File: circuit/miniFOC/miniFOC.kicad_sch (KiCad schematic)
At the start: 61 parts, among them J1 Conn_01x05, J2 Conn_01x06, J3 Conn_01x02, J4 Conn_01x01, J5 Conn_01x01, J6 Conn_01x01, U1 XC6206P332MR, U2 AT32F421C8, U3 LM321, U4 COS722MR, U5 uP9636, U6 uP9636, U7 JW5017S, U8 uP9636

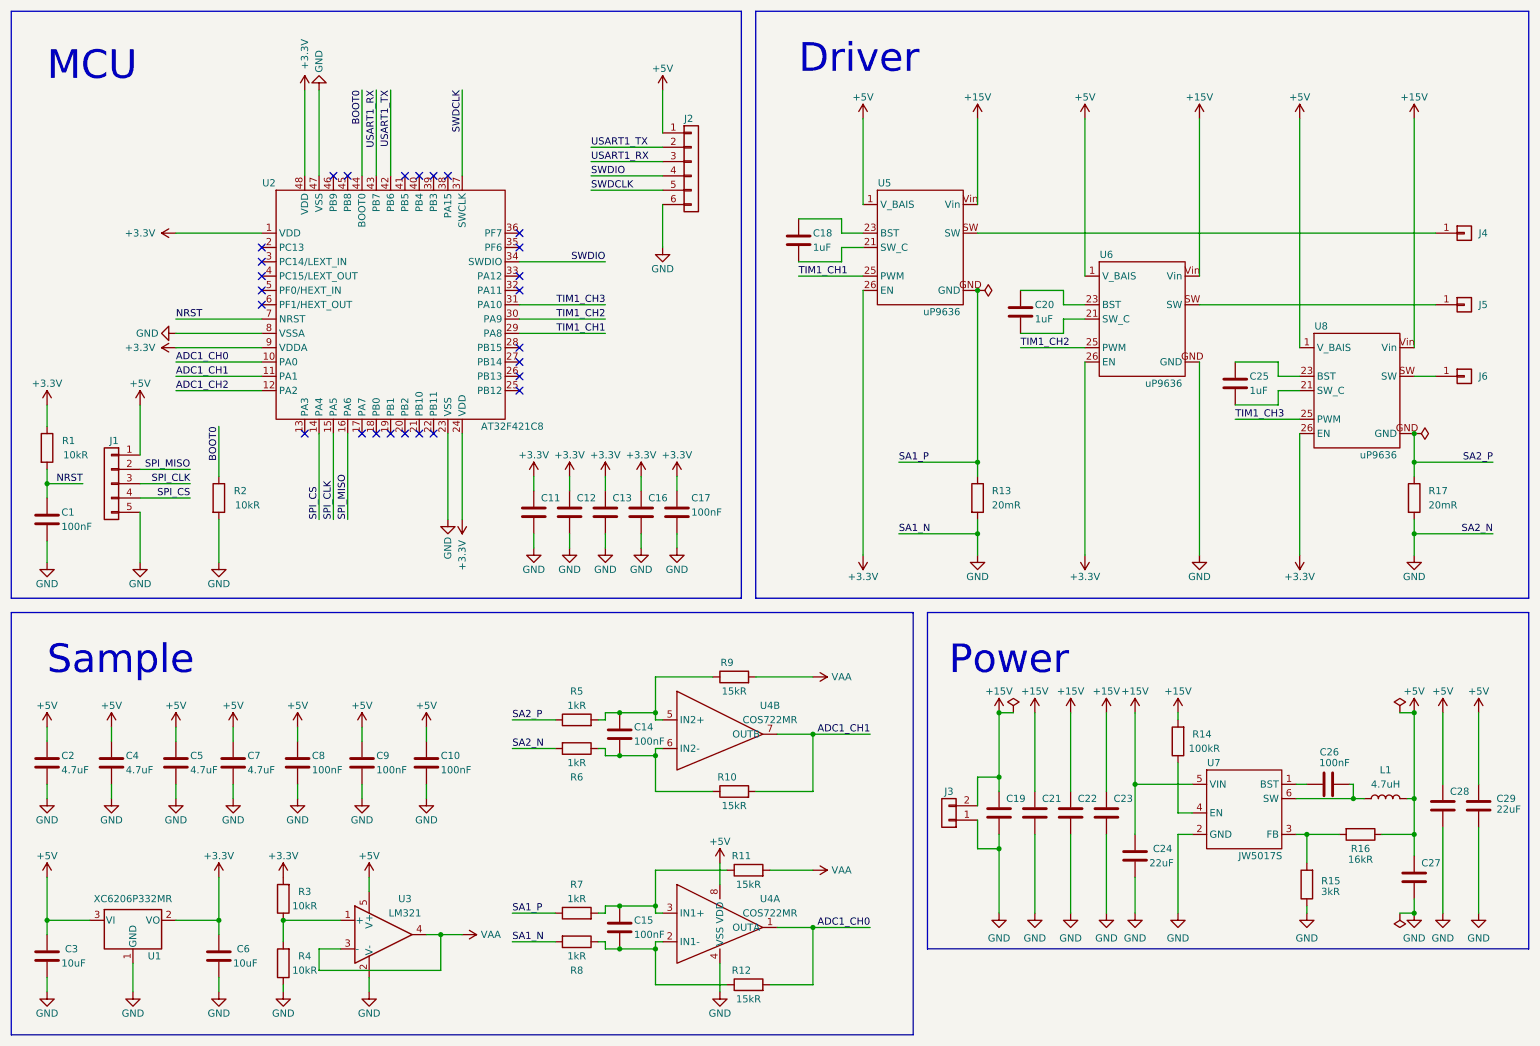
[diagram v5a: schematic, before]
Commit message: Complete the circuit and PCB design for version 2.0.
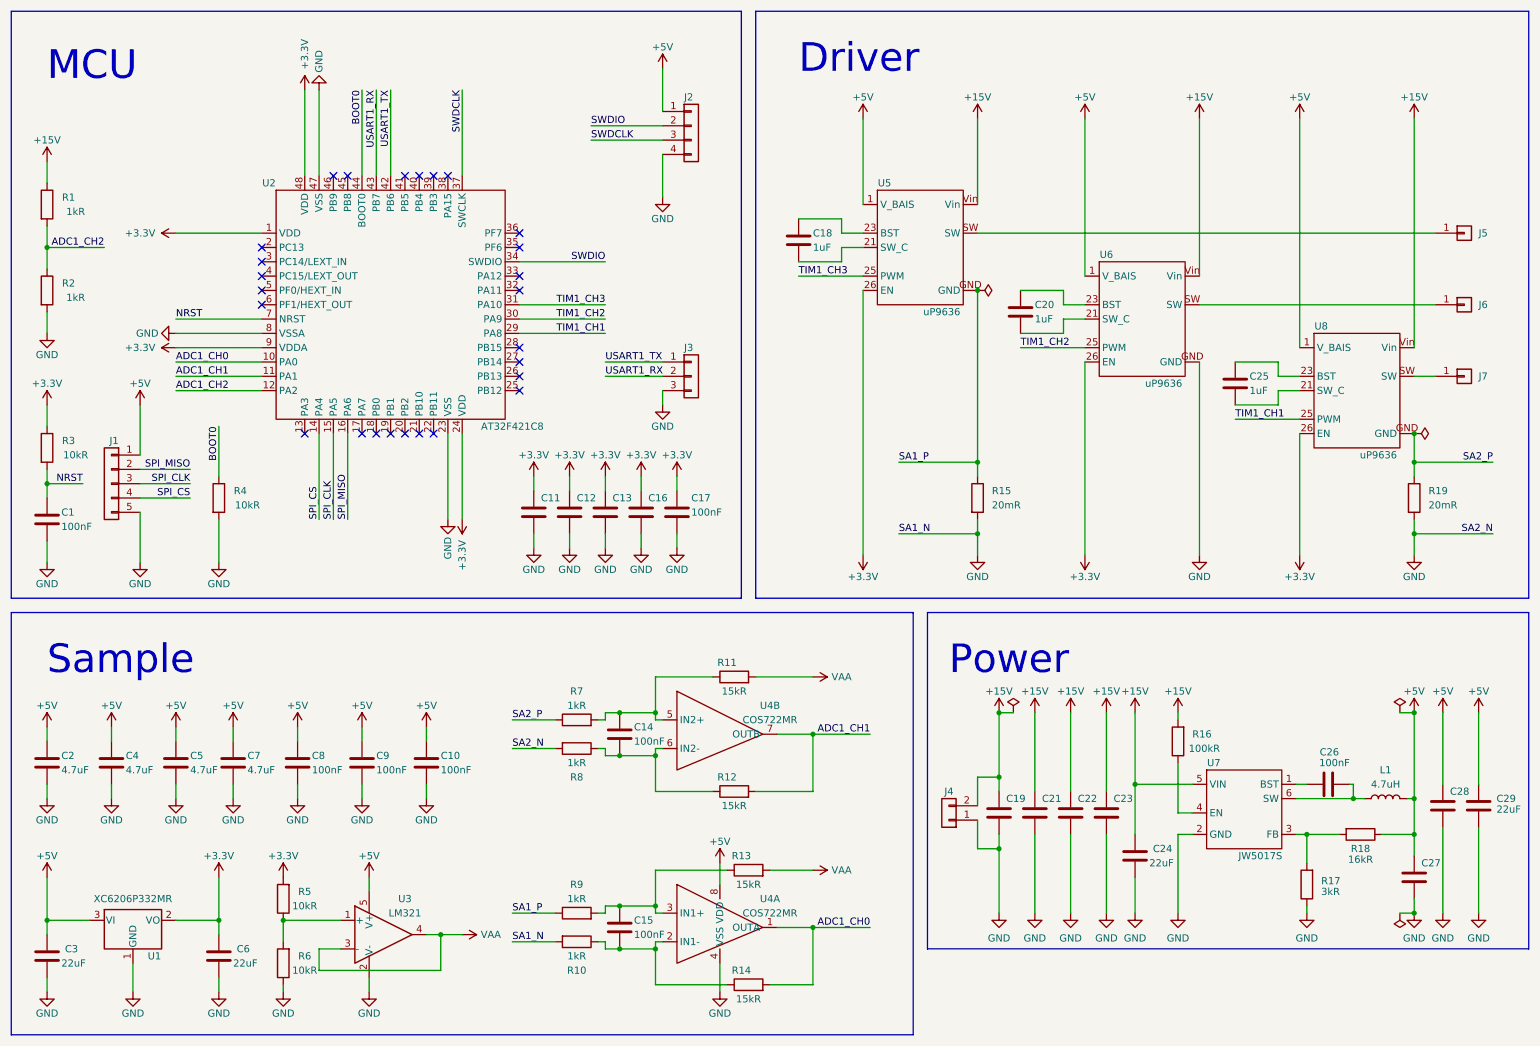
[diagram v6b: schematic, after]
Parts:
- removed J2: Conn_01x06, Connector_JST:JST_GH_SM06B-GHS-TB_1x06-1MP_P1.25mm_Horizontal, symbol Connector_Generic:Conn_01x06
- added J2: Conn_01x04, Library:Pad_4, symbol Connector_Generic:Conn_01x04
- added J3: Conn_01x03, Library:JST_GH_SM03B-GHS-TB_1x03-1MP_P1.25mm_Horizontal, symbol Connector_Generic:Conn_01x03
- added R1, R2: 1kR, Library:R_0402_1005Metric, symbol Device:R
- C1, C10, C11, C12, C13, C14, C15, C16, C17, C18, C2, C20, C25, C26, C4, C5, C7, C8, C9: footprint Capacitor_SMD:C_0402_1005Metric -> Library:C_0402_1005Metric
- C19, C21, C22, C23, C24: footprint Capacitor_SMD:C_0805_2012Metric -> Library:C_0805_2012Metric
- C27, C28, C29: footprint Capacitor_SMD:C_0603_1608Metric -> Library:C_0603_1608Metric
- C3, C6: value 10uF -> 22uF; footprint Capacitor_SMD:C_0603_1608Metric -> Library:C_0603_1608Metric
- J1: footprint Connector_JST:JST_GH_SM05B-GHS-TB_1x05-1MP_P1.25mm_Horizontal -> Library:Pad_5
- J4: renamed from J3; footprint Connector_Wire:SolderWire-0.1sqmm_1x02_P3.6mm_D0.4mm_OD1mm -> Library:SolderWire-0.1sqmm_1x02_P3.6mm_D0.4mm_OD1mm
- J5: renamed from J4; footprint Connector_PinHeader_2.54mm:PinHeader_1x01_P2.54mm_Vertical -> Library:Pad_1
- J6: renamed from J5; footprint Connector_PinHeader_2.54mm:PinHeader_1x01_P2.54mm_Vertical -> Library:Pad_1
- J7: renamed from J6; footprint Connector_PinHeader_2.54mm:PinHeader_1x01_P2.54mm_Vertical -> Library:Pad_1
- L1: footprint Inductor_SMD:L_Coilcraft_XxL4040 -> Library:L_Coilcraft_XxL4040
- R10: renamed from R8; footprint Resistor_SMD:R_0402_1005Metric -> Library:R_0402_1005Metric
- R11: renamed from R9; footprint Resistor_SMD:R_0402_1005Metric -> Library:R_0402_1005Metric
- R12: renamed from R10; footprint Resistor_SMD:R_0402_1005Metric -> Library:R_0402_1005Metric
- R13: renamed from R11; footprint Resistor_SMD:R_0402_1005Metric -> Library:R_0402_1005Metric
- R14: renamed from R12; footprint Resistor_SMD:R_0402_1005Metric -> Library:R_0402_1005Metric
- R15: renamed from R13; footprint Resistor_SMD:R_0805_2012Metric -> Library:R_0805_2012Metric
- R16: renamed from R14; footprint Capacitor_SMD:C_0402_1005Metric -> Library:R_0402_1005Metric
- R17: renamed from R15; footprint Capacitor_SMD:C_0402_1005Metric -> Library:R_0402_1005Metric
- R18: renamed from R16; footprint Capacitor_SMD:C_0402_1005Metric -> Library:R_0402_1005Metric
- R19: renamed from R17; footprint Resistor_SMD:R_0805_2012Metric -> Library:R_0805_2012Metric
- R3: renamed from R1; footprint Resistor_SMD:R_0402_1005Metric -> Library:R_0402_1005Metric
- R4: renamed from R2; footprint Resistor_SMD:R_0402_1005Metric -> Library:R_0402_1005Metric
- R5: renamed from R3; footprint Resistor_SMD:R_0402_1005Metric -> Library:R_0402_1005Metric
- R6: renamed from R4; footprint Resistor_SMD:R_0402_1005Metric -> Library:R_0402_1005Metric
- R7: renamed from R5; footprint Resistor_SMD:R_0402_1005Metric -> Library:R_0402_1005Metric
- R8: renamed from R6; footprint Resistor_SMD:R_0402_1005Metric -> Library:R_0402_1005Metric
- R9: renamed from R7; footprint Resistor_SMD:R_0402_1005Metric -> Library:R_0402_1005Metric
- U1: footprint Package_TO_SOT_SMD:SOT-23 -> Library:SOT-23
- U2: footprint Package_QFP:LQFP-48_7x7mm_P0.5mm -> Library:LQFP-48_7x7mm_P0.5mm
- U3: footprint Package_TO_SOT_SMD:SOT-23-5 -> Library:SOT-23-5
- U4: footprint Package_SO:MSOP-8_3x3mm_P0.65mm -> Library:MSOP-8_3x3mm_P0.65mm
- U7: footprint Package_TO_SOT_SMD:SOT-23-6 -> Library:SOT-23-6
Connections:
- net +15V: now also R1.1
- net +5V: now also J2.1 (Pin_1)
- net ADC1_CH2: now also R1.2, R2.1
- net GND: now also J2.4 (Pin_4), J3.3 (Pin_3), R2.2
- net SWDCLK: now also J2.3 (Pin_3)
- net SWDIO: now also J2.2 (Pin_2)
- net TIM1_CH1: now also U8.25 (PWM); no longer U5.25 (PWM)
- net TIM1_CH3: now also U5.25 (PWM); no longer U8.25 (PWM)
- net USART1_RX: now also J3.2 (Pin_2)
- net USART1_TX: now also J3.1 (Pin_1)

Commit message: Mosify miniFOC schematic, using new scheme
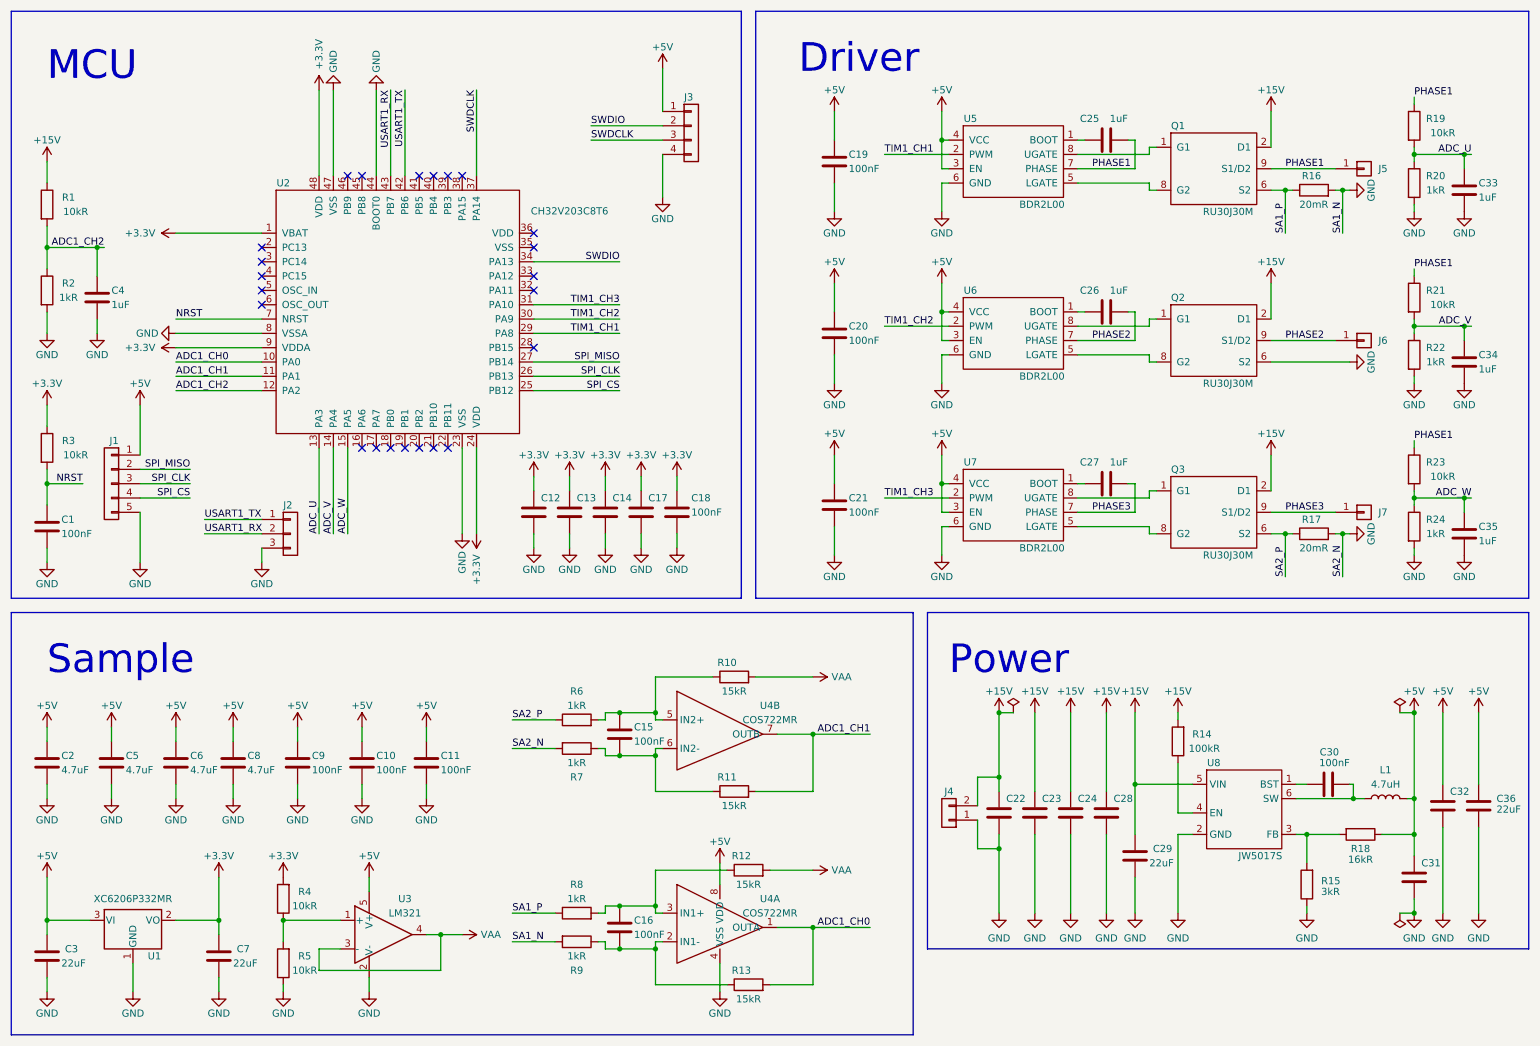
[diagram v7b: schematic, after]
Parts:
- removed C18, C20, C25: 1uF, Library:C_0402_1005Metric, symbol Device:C
- removed R19: 20mR, Library:R_0805_2012Metric, symbol Device:R
- removed R4: 10kR, Library:R_0402_1005Metric, symbol Device:R
- removed U2: AT32F421C8, Library:LQFP-48_7x7mm_P0.5mm, symbol Library:AT32F421C8
- removed U5, U6, U8: uP9636, Library:QFN-26_4040_IPS, symbol Library:uP9636
- added C19, C20, C21: 100nF, library:C_0402_1005Metric, symbol library:C
- added C25, C26, C27, C33, C34, C35, C4: 1uF, library:C_0402_1005Metric, symbol library:C
- added Q1, Q2, Q3: RU30J30M, library:PDFN-8_L5.8-W4.9_RU30J30M, symbol library:RU30J30M
- added R17: 20mR, library:R_0805_2012Metric, symbol library:R
- added R19, R21, R23: 10kR, library:R_0402_1005Metric, symbol library:R
- added R20, R22, R24: 1kR, library:R_0402_1005Metric, symbol library:R
- added U2: CH32V203C8T6, library:LQFP-48_7x7mm_P0.5mm, symbol library:CH32V203C8T6
- added U5, U6, U7: BDR2L00, library:TDFN-8_L2.0-W2.0-P0.50-BL-EP, symbol library:BDR2L00
- C1, C2: footprint Library:C_0402_1005Metric -> library:C_0402_1005Metric; symbol Device:C -> library:C
- C10: renamed from C9; footprint Library:C_0402_1005Metric -> library:C_0402_1005Metric; symbol Device:C -> library:C
- C11: renamed from C10; footprint Library:C_0402_1005Metric -> library:C_0402_1005Metric; symbol Device:C -> library:C
- C12: renamed from C11; footprint Library:C_0402_1005Metric -> library:C_0402_1005Metric; symbol Device:C -> library:C
- C13: renamed from C12; footprint Library:C_0402_1005Metric -> library:C_0402_1005Metric; symbol Device:C -> library:C
- C14: renamed from C13; footprint Library:C_0402_1005Metric -> library:C_0402_1005Metric; symbol Device:C -> library:C
- C15: renamed from C14; footprint Library:C_0402_1005Metric -> library:C_0402_1005Metric; symbol Device:C -> library:C
- C16: renamed from C15; footprint Library:C_0402_1005Metric -> library:C_0402_1005Metric; symbol Device:C -> library:C
- C17: renamed from C16; footprint Library:C_0402_1005Metric -> library:C_0402_1005Metric; symbol Device:C -> library:C
- C18: renamed from C17; footprint Library:C_0402_1005Metric -> library:C_0402_1005Metric; symbol Device:C -> library:C
- C22: renamed from C19; footprint Library:C_0805_2012Metric -> library:C_0805_2012Metric; symbol Device:C -> library:C
- C23: renamed from C21; footprint Library:C_0805_2012Metric -> library:C_0805_2012Metric; symbol Device:C -> library:C
- C24: renamed from C22; footprint Library:C_0805_2012Metric -> library:C_0805_2012Metric; symbol Device:C -> library:C
- C28: renamed from C23; footprint Library:C_0805_2012Metric -> library:C_0805_2012Metric; symbol Device:C -> library:C
- C29: renamed from C24; footprint Library:C_0805_2012Metric -> library:C_0805_2012Metric; symbol Device:C -> library:C
- C3: footprint Library:C_0603_1608Metric -> library:C_0603_1608Metric; symbol Device:C -> library:C
- C30: renamed from C26; footprint Library:C_0402_1005Metric -> library:C_0402_1005Metric; symbol Device:C -> library:C
- C31: renamed from C27; footprint Library:C_0603_1608Metric -> library:C_0603_1608Metric; symbol Device:C -> library:C
- C32: renamed from C28; footprint Library:C_0603_1608Metric -> library:C_0603_1608Metric; symbol Device:C -> library:C
- C36: renamed from C29; footprint Library:C_0603_1608Metric -> library:C_0603_1608Metric; symbol Device:C -> library:C
- C5: renamed from C4; footprint Library:C_0402_1005Metric -> library:C_0402_1005Metric; symbol Device:C -> library:C
- C6: renamed from C5; footprint Library:C_0402_1005Metric -> library:C_0402_1005Metric; symbol Device:C -> library:C
- C7: renamed from C6; footprint Library:C_0603_1608Metric -> library:C_0603_1608Metric; symbol Device:C -> library:C
- C8: renamed from C7; footprint Library:C_0402_1005Metric -> library:C_0402_1005Metric; symbol Device:C -> library:C
- C9: renamed from C8; footprint Library:C_0402_1005Metric -> library:C_0402_1005Metric; symbol Device:C -> library:C
- J1: footprint Library:Pad_5 -> library:Pad_5; symbol Connector_Generic:Conn_01x05 -> library:Conn_01x05
- J2: renamed from J3; footprint Library:JST_GH_SM03B-GHS-TB_1x03-1MP_P1.25mm_Horizontal -> library:JST_GH_SM03B-GHS-TB_1x03-1MP_P1.25mm_Horizontal; symbol Connector_Generic:Conn_01x03 -> library:Conn_01x03
- J3: renamed from J2; footprint Library:Pad_4 -> library:Pad_4; symbol Connector_Generic:Conn_01x04 -> library:Conn_01x04
- J4: footprint Library:SolderWire-0.1sqmm_1x02_P3.6mm_D0.4mm_OD1mm -> library:SolderWire-0.1sqmm_1x02_P3.6mm_D0.4mm_OD1mm; symbol Connector_Generic:Conn_01x02 -> library:Conn_01x02
- J5, J6, J7: footprint Library:Pad_1 -> library:Pad_1; symbol Connector_Generic:Conn_01x01 -> library:Conn_01x01
- L1: footprint Library:L_Coilcraft_XxL4040 -> library:L_Coilcraft_XxL4040; symbol Device:L -> library:L
- R1: value 1kR -> 10kR; footprint Library:R_0402_1005Metric -> library:R_0402_1005Metric; symbol Device:R -> library:R
- R10: renamed from R11; footprint Library:R_0402_1005Metric -> library:R_0402_1005Metric; symbol Device:R -> library:R
- R11: renamed from R12; footprint Library:R_0402_1005Metric -> library:R_0402_1005Metric; symbol Device:R -> library:R
- R12: renamed from R13; footprint Library:R_0402_1005Metric -> library:R_0402_1005Metric; symbol Device:R -> library:R
- R13: renamed from R14; footprint Library:R_0402_1005Metric -> library:R_0402_1005Metric; symbol Device:R -> library:R
- R14: renamed from R16; footprint Library:R_0402_1005Metric -> library:R_0402_1005Metric; symbol Device:R -> library:R
- R15: renamed from R17; footprint Library:R_0402_1005Metric -> library:R_0402_1005Metric; symbol Device:R -> library:R
- R16: renamed from R15; footprint Library:R_0805_2012Metric -> library:R_0805_2012Metric; symbol Device:R -> library:R
- R18, R2, R3: footprint Library:R_0402_1005Metric -> library:R_0402_1005Metric; symbol Device:R -> library:R
- R4: renamed from R5; footprint Library:R_0402_1005Metric -> library:R_0402_1005Metric; symbol Device:R -> library:R
- R5: renamed from R6; footprint Library:R_0402_1005Metric -> library:R_0402_1005Metric; symbol Device:R -> library:R
- R6: renamed from R7; footprint Library:R_0402_1005Metric -> library:R_0402_1005Metric; symbol Device:R -> library:R
- R7: renamed from R8; footprint Library:R_0402_1005Metric -> library:R_0402_1005Metric; symbol Device:R -> library:R
- R8: renamed from R9; footprint Library:R_0402_1005Metric -> library:R_0402_1005Metric; symbol Device:R -> library:R
- R9: renamed from R10; footprint Library:R_0402_1005Metric -> library:R_0402_1005Metric; symbol Device:R -> library:R
- U1: footprint Library:SOT-23 -> library:SOT-23; symbol Regulator_Linear:XC6206PxxxMR -> library:XC6206PxxxMR
- U3: footprint Library:SOT-23-5 -> library:SOT-23-5; symbol Amplifier_Operational:LM321 -> library:LM321
- U4: footprint Library:MSOP-8_3x3mm_P0.65mm -> library:MSOP-8_3x3mm_P0.65mm; symbol Library:COS722MR -> library:COS722MR
- U8: renamed from U7; footprint Library:SOT-23-6 -> library:SOT-23-6; symbol power_Library:JW5017S -> library:JW5017S
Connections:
- net +15V: now also Q1.2 (D1), Q1.3 (D1), Q1.4 (D1), Q2.2 (D1), Q2.3 (D1), Q2.4 (D1), Q3.2 (D1), Q3.3 (D1), Q3.4 (D1)
- net +3.3V: now also U2.1 (VBAT), U2.24 (VDD), U2.48 (VDD), U2.9 (VDDA)
- net +5V: now also C19.1, C20.1, C21.1, U5.3 (EN), U5.4 (VCC), U6.3 (EN), U6.4 (VCC), U7.3 (EN), U7.4 (VCC)
- net ADC1_CH0: now also U2.10 (PA0)
- net ADC1_CH1: now also U2.11 (PA1)
- net ADC1_CH2: now also C4.1, U2.12 (PA2)
- net NRST: now also U2.7 (NRST)
- net SA1_P: now also Q1.5 (S2), Q1.6 (S2), Q1.7 (S2)
- net SA2_P: now also Q3.5 (S2), Q3.6 (S2), Q3.7 (S2), R17.1
- net SPI_CLK: now also U2.26 (PB13)
- net SPI_CS: now also U2.25 (PB12)
- net SPI_MISO: now also U2.27 (PB14)
- net SWDCLK: now also U2.37 (PA14)
- net SWDIO: now also U2.34 (PA13)
- net TIM1_CH1: now also U2.29 (PA8), U5.2 (PWM)
- net TIM1_CH2: now also U2.30 (PA9), U6.2 (PWM)
- net TIM1_CH3: now also U2.31 (PA10), U7.2 (PWM)
- net USART1_RX: now also U2.43 (PB7)
- net USART1_TX: now also U2.42 (PB6)
- net PHASE3: now reaches J7.1 (Pin_1)
- net PHASE3: now also C27.2, Q3.9 (S1/D2), U7.7 (PHASE)
- net PHASE1: now reaches J5.1 (Pin_1)
- net PHASE1: now also C25.2, Q1.9 (S1/D2), R19.1, R21.1, R23.1, U5.7 (PHASE)
- net PHASE2: now reaches J6.1 (Pin_1)
- net PHASE2: now also C26.2, Q2.9 (S1/D2), U6.7 (PHASE)
- net GND renamed EP
- net EP: now also C19.2, C20.2, C21.2, C33.2, C34.2, C35.2, C4.2, Q2.5 (S2), Q2.6 (S2), Q2.7 (S2), R17.2, R20.2, R22.2, R24.2, U2.23 (VSS), U2.44 (BOOT0), U2.47 (VSS), U2.8 (VSSA), U5.6 (GND), U5.9 (EP), U6.6 (GND), U6.9 (EP), U7.6 (GND), U7.9 (EP)
- new net: C26.1, U6.1 (BOOT)
- new net: C25.1, U5.1 (BOOT)
- new net: Q1.8 (G2), U5.5 (LGATE)
- new net: Q1.1 (G1), U5.8 (UGATE)
- new net: Q2.1 (G1), U6.8 (UGATE)
- new net: Q2.8 (G2), U6.5 (LGATE)
- new net: C27.1, U7.1 (BOOT)
- new net: Q3.8 (G2), U7.5 (LGATE)
- new net: Q3.1 (G1), U7.8 (UGATE)
- new net ADC_U: C33.1, R19.2, R20.1, U2.13 (PA3)
- new net ADC_V: C34.1, R21.2, R22.1, U2.14 (PA4)
- new net ADC_W: C35.1, R23.2, R24.1, U2.15 (PA5)
- no-connect marks 26 -> 23
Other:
- moved on the sheet: C1, J2, J5, J6, J7, R16
